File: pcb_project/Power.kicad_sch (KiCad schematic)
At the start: 53 parts, among them IC1 TPS54325PWPR, IC2 TPS54294PWPR, J10 M20-9990246, J11 M20-9990246, J12 M20-9990246, J5 USB_B_Micro, J9 M20-9990246, Q3 MMBT3904LT1G, Q4 MMBT3904LT1G

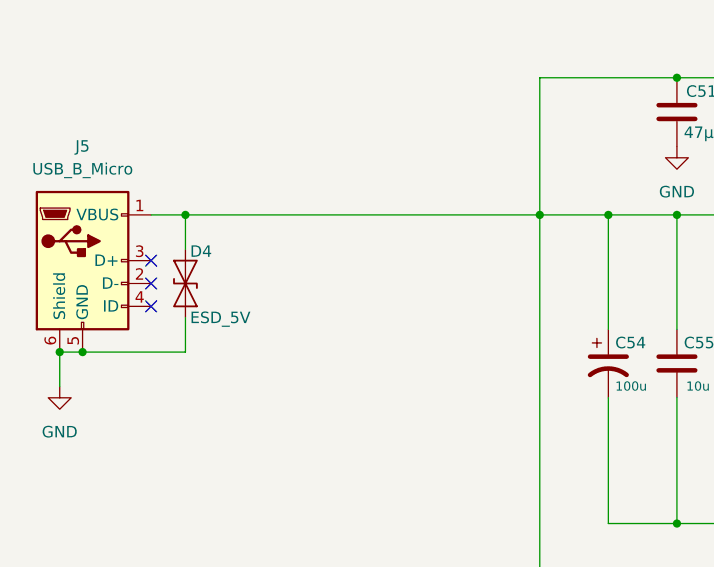
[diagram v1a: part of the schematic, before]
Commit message: Remove Power esd diode
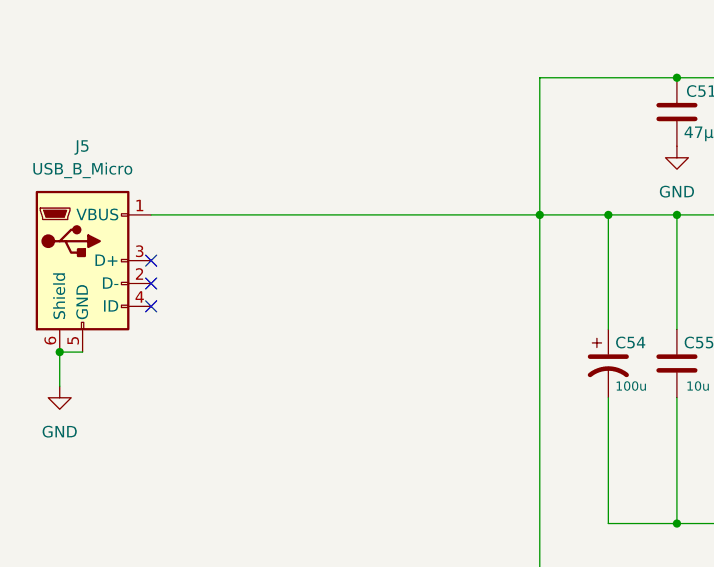
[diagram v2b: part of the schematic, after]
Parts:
- removed D4: ESD_5V, Diode_SMD:D_SOD-923, symbol Diode:ESD9B5.0ST5G
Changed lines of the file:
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@@
-	)
-	(junction
-		(at 50.8 35.56)
-		(diameter 0)
-		(color 0 0 0 0)
 	)
 	(junction
@@
 	(junction
 		(at 217.17 130.81)
-		(diameter 0)
-		(color 0 0 0 0)
-	)
-	(junction
-		(at 39.37 50.8)
 		(diameter 0)
 		(color 0 0 0 0)
@@
 	(wire
 		(pts
-			(xy 50.8 35.56) (xy 90.17 35.56)
+			(xy 46.99 35.56) (xy 90.17 35.56)
 		)
 		(stroke
@@
 	(wire
 		(pts
-			(xy 50.8 46.99) (xy 50.8 50.8)
-		)
-		(stroke
-			(width 0)
-			(type default)
-		)
-	)
-	(wire
-		(pts
 			(xy 193.04 48.26) (xy 204.47 48.26)
 		)
@@
 	(wire
 		(pts
-			(xy 50.8 35.56) (xy 50.8 39.37)
-		)
-		(stroke
-			(width 0)
-			(type default)
-		)
-	)
-	(wire
-		(pts
 			(xy 128.27 35.56) (xy 128.27 38.1)
 		)
@@
 	(wire
 		(pts
-			(xy 46.99 35.56) (xy 50.8 35.56)
-		)
-		(stroke
-			(width 0)
-			(type default)
-		)
-	)
-	(wire
-		(pts
 			(xy 166.37 115.57) (xy 166.37 118.11)
 		)
@@
 		(pts
 			(xy 105.41 55.88) (xy 105.41 69.85)
-		)
-		(stroke
-			(width 0)
-			(type default)
-		)
-	)
-	(wire
-		(pts
-			(xy 39.37 50.8) (xy 50.8 50.8)
 		)
 		(stroke
@@
 					(unit 1)
 				)
-			)
-		)
-	)
-	(symbol
-		(lib_id "Diode:ESD9B5.0ST5G")
-		(at 50.8 43.18 90)
-		(unit 1)
-		(exclude_from_sim no)
-		(in_bom yes)
-		(on_board yes)
-		(dnp no)
-		(property "Reference" "D4"
-			(at 51.308 39.624 90)
-			(effects
-				(font
-					(size 1.27 1.27)
-				)
-				(justify right)
-			)
-		)
-		(property "Value" "ESD_5V"
-			(at 51.308 46.99 90)
-			(effects
-				(font
-					(size 1.27 1.27)
-				)
-				(justify right)
-			)
-		)
-		(property "Footprint" "Diode_SMD:D_SOD-923"
-			(at 50.8 43.18 0)
-			(effects
-				(font
-					(size 1.27 1.27)
-				)
-				(hide yes)
-			)
-		)
-		(property "Datasheet" "https://www.onsemi.com/pub/Collateral/ESD9B-D.PDF"
-			(at 50.8 43.18 0)
-			(effects
-				(font
-					(size 1.27 1.27)
-				)
-				(hide yes)
-			)
-		)
-		(property "Description" "ESD protection diode, 5.0Vrwm, SOD-923"
-			(at 50.8 43.18 0)
-			(effects
-				(font
-					(size 1.27 1.27)
-				)
-				(hide yes)
-			)
-		)
-		(property "Sim.Pins" ""
-			(at 50.8 43.18 90)
-			(effects
-				(font
-					(size 1.27 1.27)
-				)
-				(hide yes)
-			)
-		)
-		(pin "2"
-		)
-		(pin "1"
-		)
-		(instances
-			(project ""
-				(path "/98f80f66-4595-4d0f-90ca-59b2db6f447b/ce445763-774c-4caf-b911-9c6f9b75d87a"
-					(reference "D4")
-					(unit 1)
-				)

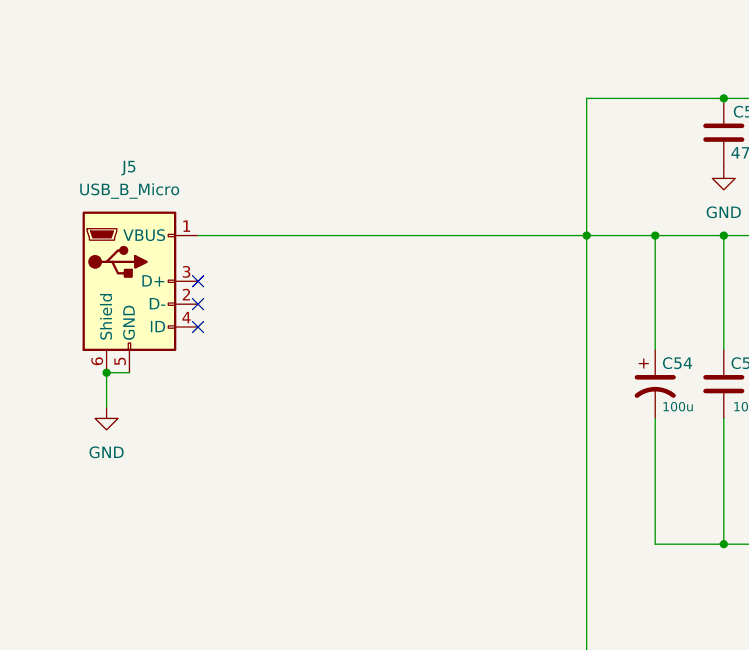
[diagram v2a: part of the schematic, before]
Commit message: Update MicroUSB symbol and edit footprint to match constraints
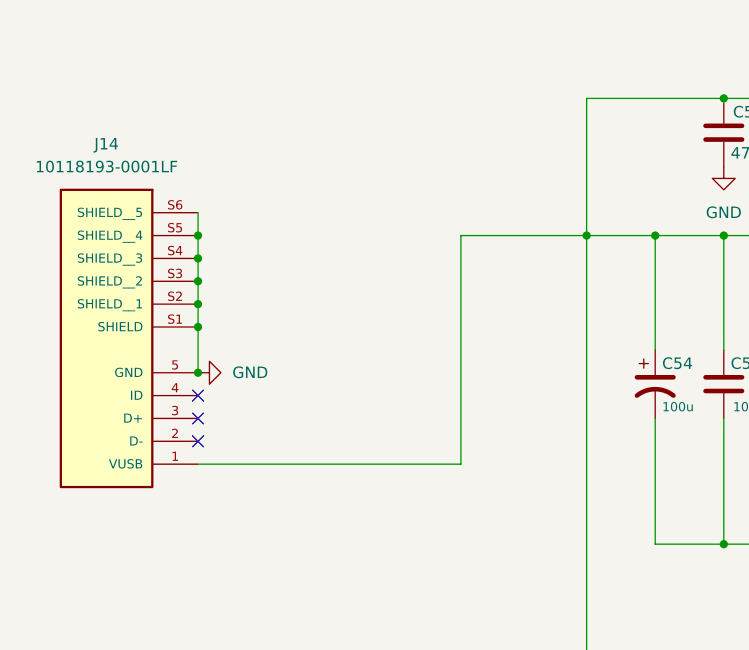
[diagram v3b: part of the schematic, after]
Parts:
- removed J5: USB_B_Micro, Connector_USB:USB_Micro-B_Amphenol_10103594-0001LF_Horizontal, symbol Connector:USB_B_Micro
- added J14: 10118193-0001LF, Project_Footprints:AMPHENOL_10118193-0001LF, symbol 10118193-0001LF:10118193-0001LF
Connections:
- net GND: now also J14.5 (GND), J14.S1 (SHIELD), J14.S2 (SHIELD__1), J14.S3 (SHIELD__2), J14.S4 (SHIELD__3), J14.S5 (SHIELD__4), J14.S6 (SHIELD__5)
- net at C51.1, C54.1, C55.1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: now also J14.1 (VUSB)
